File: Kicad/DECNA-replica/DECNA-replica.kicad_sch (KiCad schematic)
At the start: 94 parts, among them J10 BDAL08, J11 BDAL09, J12 BDAL10, J13 BDAL11, J14 BDAL12, J15 BDAL13, J16 BDAL14, J17 BDAL15, J18 BDAL16, J19 BDAL17, J2 BDAL00, J20 BDAL18, J21 BDAL19, J22 BDAL20, J23 BDAL21, J24 BRPLYL, J25 BMDENL, J26 BWRITEL, J27 BWLBL, J28 BWHBL, J29 BSDENL, J3 BDAL01, J30 SSnL, J31 BDSL, J32 BASL, J33 BIOSELL, J34 BDCOKH, J35 GND, J36 GND, J37 GND, J38 DAH00, J39 DAH01, J4 BDAL02, J40 DAH02, J41 DAH03, J42 DAH04, J43 DAH05, J44 DAH06, J45 DAH07, J46 DAH08, J47 DAH09, J48 DAH10, J49 DAH11, J5 BDAL03, J50 DAH12, J51 DAH13, J52 DAH14, J53 DAH15, J54 DAH16, J55 DAH17, J56 DAH18, J57 DAH19, J58 DAH20, J59 DAH21, J6 BDAL04, J60 ASL, J61 MDENL, J62 SDENL, J63 MOEL, J64 MWEL, J65 MCEHIGHL, J66 MCELOWH, J67 MLEL, J68 MHEL, J69 BUSDIR, J7 BDAL05, J70 BUSOE, J71 CLK, J72 MA15, J73 MA16, J74 MA17, J75 MA18, J76 MA19, J77 MA20, J78 MA21, J79 HOLDL, J8 BDAL06, J80 CSL, J81 JTAG, J9 BDAL07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

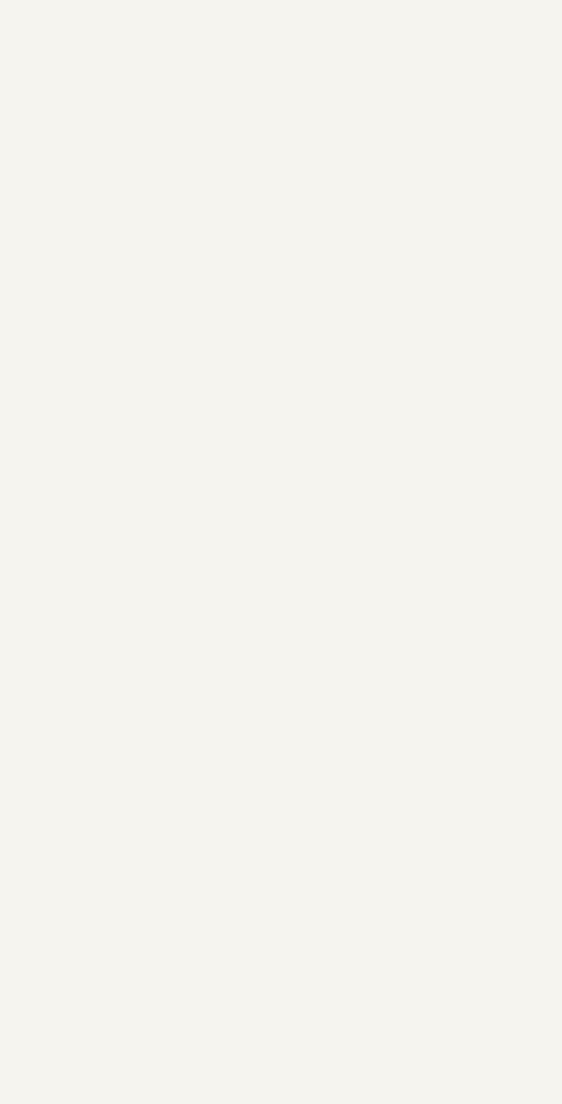
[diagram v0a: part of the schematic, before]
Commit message: Added some symbols.
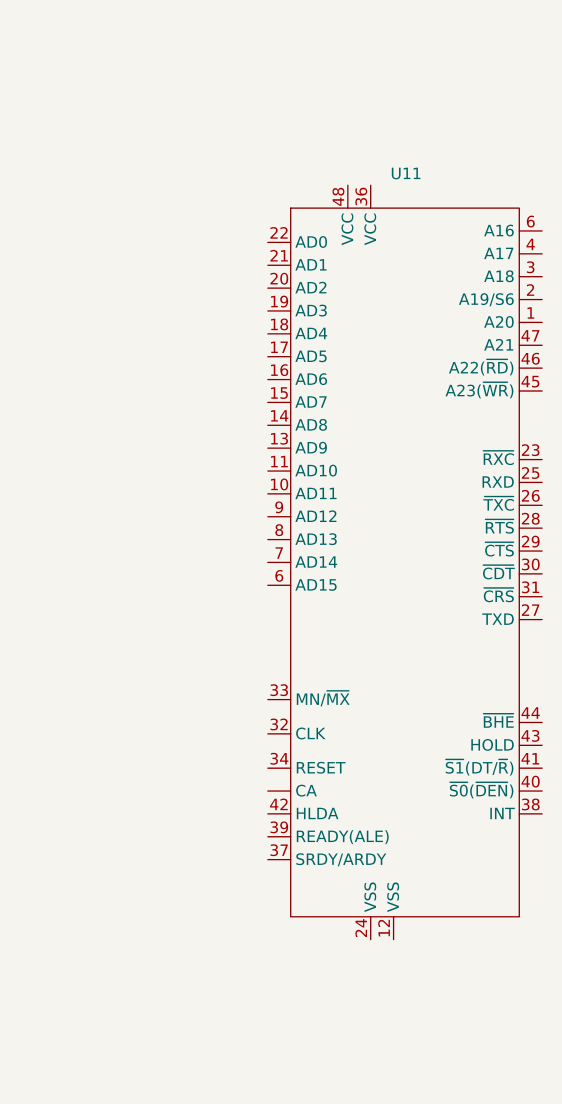
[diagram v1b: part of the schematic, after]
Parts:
- added U11: ~, Package_DIP:DIP-48_W15.24mm, symbol DECNA:82586
